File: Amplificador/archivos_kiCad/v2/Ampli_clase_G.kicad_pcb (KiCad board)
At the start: 2 copper layers, 132 x 112.1 mm, 121 parts, among them J1 Conn_IN, J2 LOAD_CONN, J3 SUPPLY_CONN, J4 CONN_OUT, Q1 BC856, Q10 BC846, Q11 2SC4793, Q14 2SC4793, Q15 2SA1837, Q16 2SC4793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

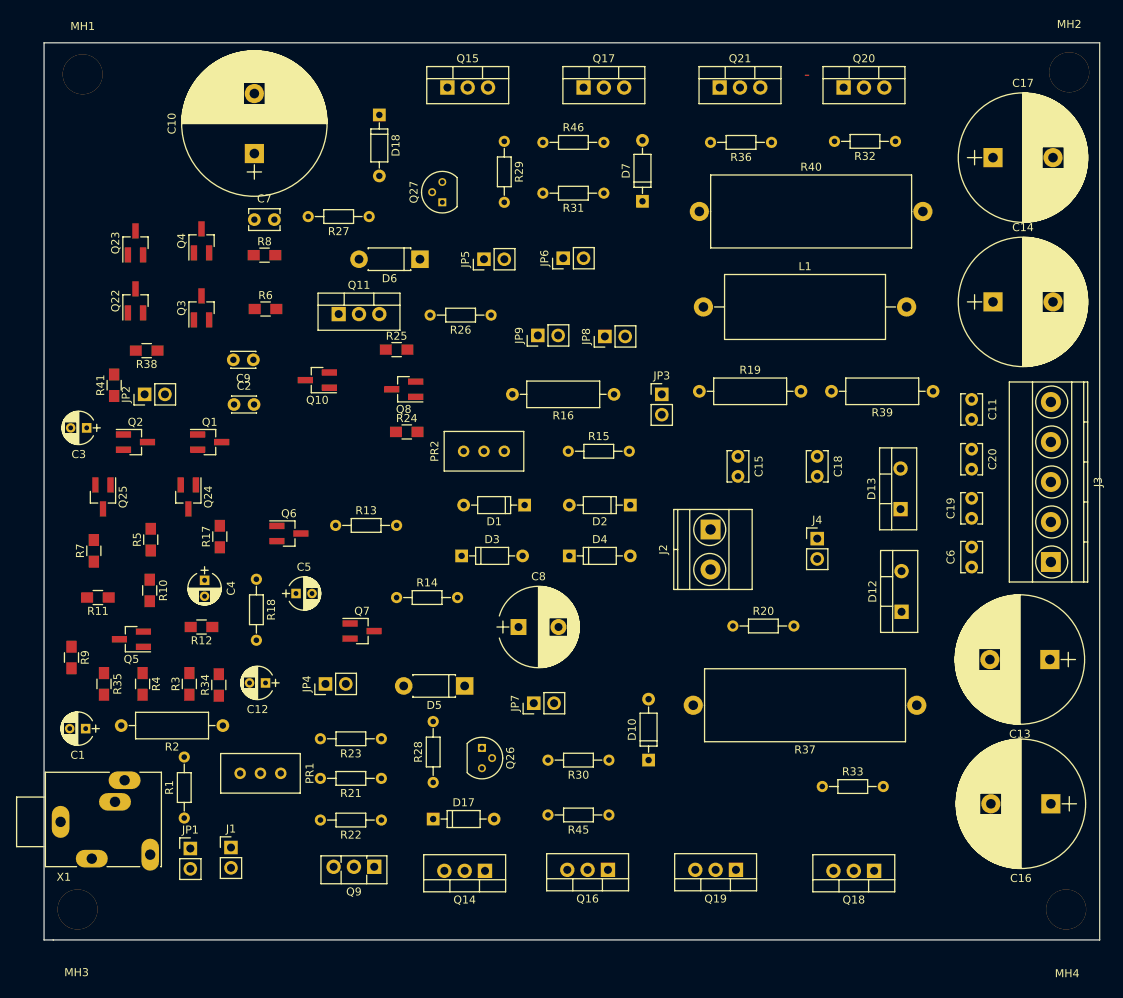
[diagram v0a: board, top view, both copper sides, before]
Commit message: Archivos de KiCad - Correccion de transistor Q7
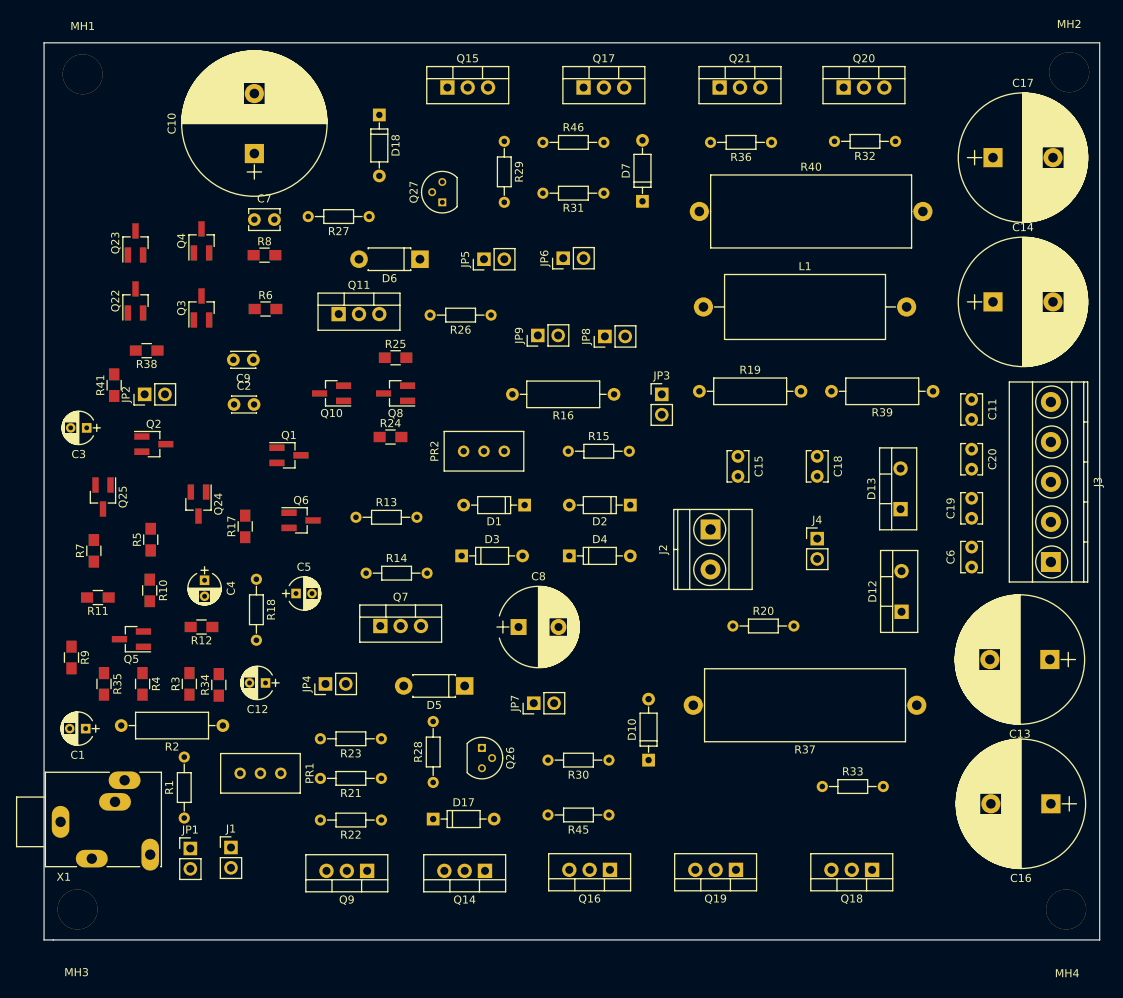
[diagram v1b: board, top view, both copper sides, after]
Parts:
- Q7: value BC856 -> 2SC4793; footprint TO_SOT_Packages_SMD:SOT-23_Handsoldering -> TO_SOT_Packages_THT:TO-220-3_Vertical
- Q9: footprint TO_SOT_Packages_THT:TO-126_Vertical -> TO_SOT_Packages_THT:TO-220-3_Vertical
- moved Q1 10.0 mm to (85.5, 79.0)
- moved R14 4.88 mm to (95.1, 93.7)
- moved R17 3.42 mm to (80.0, 87.9)
- moved R13 2.74 mm to (93.9, 86.7)
- moved Q10 2.43 mm to (90.8, 71.2)
- moved Q7 2.37 mm to (96.9, 100.3)
- moved Q2 2.30 mm to (68.6, 77.6)
- moved Q6 2.25 mm to (87.0, 87.1)
- moved R24 2.13 mm to (98.2, 76.7)
- moved Q24 1.55 mm to (74.2, 85.1)
- moved Q8 1.14 mm to (98.8, 71.2)
- moved R25 1.02 mm to (98.8, 66.8)
- moved Q9 1.02 mm to (95.2, 130.9)
- moved Q18 0.28 mm to (158.4, 130.8)
- moved Q16 0.25 mm to (125.6, 130.8)
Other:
- board text removed: "-"
